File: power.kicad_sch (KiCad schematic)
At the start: 29 parts, among them U201 XC6206PxxxMR, U202 XR76208

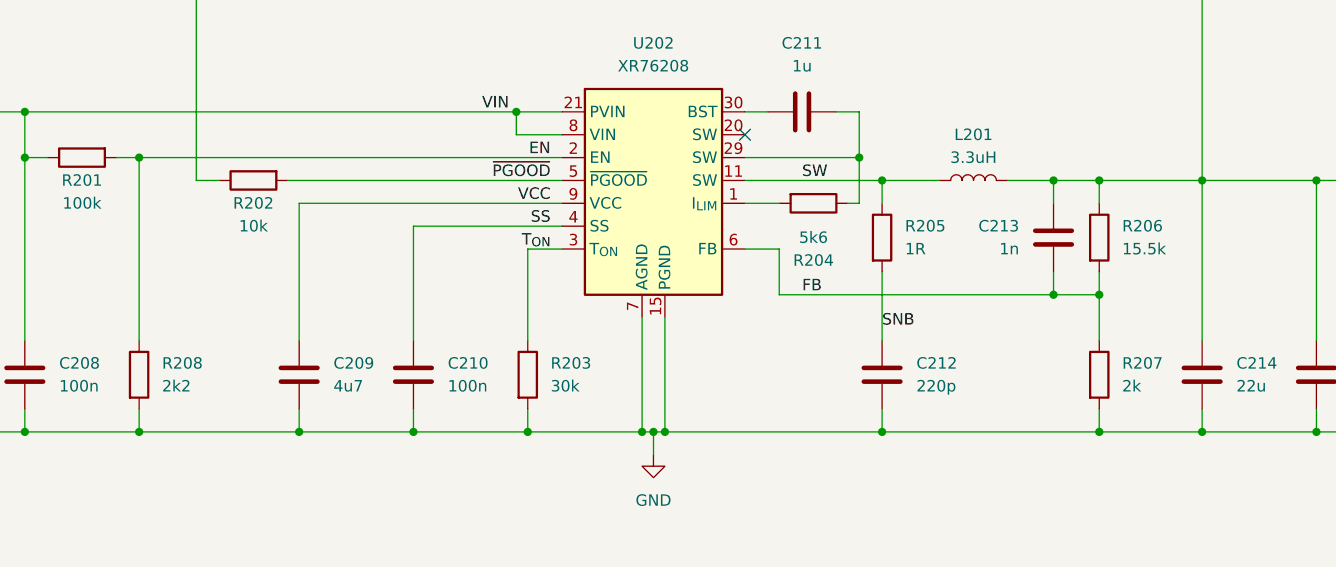
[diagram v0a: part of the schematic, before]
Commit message: Major hardware update: toolhead switching, DC/DC protection, and documentation overhaul
Hardware Changes:
- Replaced reverse polarity protection with 2x PFET toolhead switching (PB2/PA5 control)
- Added SS56 Schottky diode reverse polarity protection for DC/DC converter
- Updated current limit resistor to 5.1kΩ (~10.2A)
- Removed fan control circuitry and JST-XH connector
- Removed internal JST-XH USB port with fuse/protection

Documentation Updates:
- Updated both README files to reflect hardware changes
- Removed all fan control references and configurations
- Updated Klipper configuration examples
- Cleaned up pinout and connector assignments
- Updated technical specifications table
- Fixed table of contents and cross-references
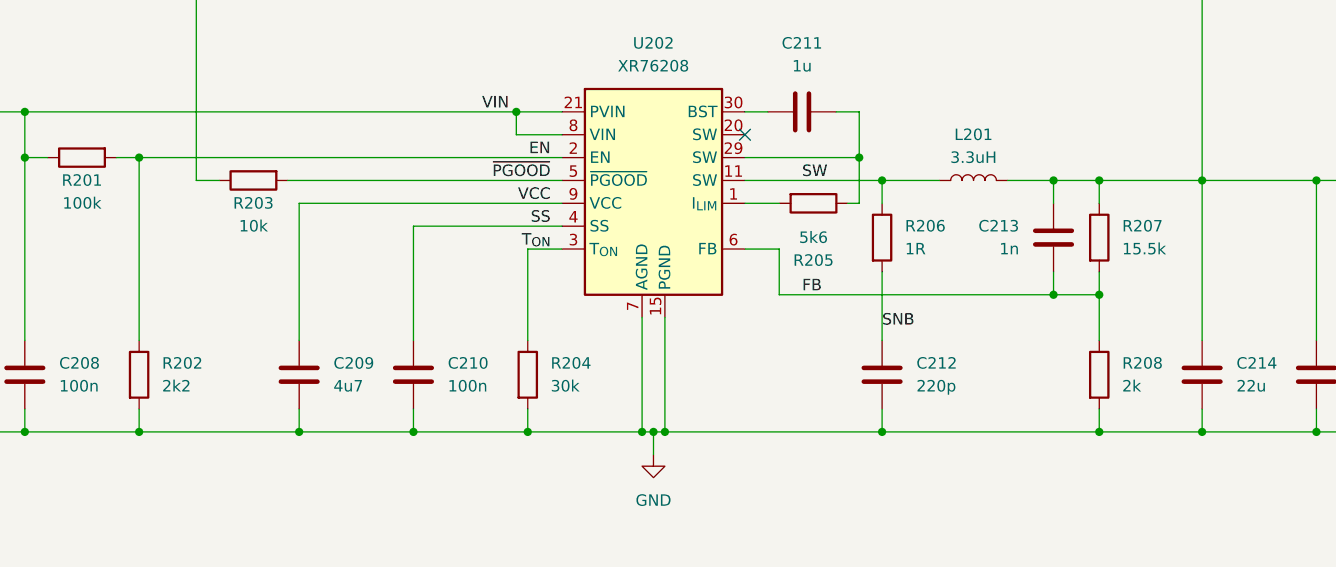
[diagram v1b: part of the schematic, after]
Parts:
- renumbered R208 to R202, R202 to R203, R203 to R204, R204 to R205, R205 to R206, R206 to R207, R207 to R208
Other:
- company: (none) -> Eduard Iten
- title: (none) -> EWS - Power, CANbus and USB HAT for 3D Printers
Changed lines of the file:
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@@
 	(generator_version "9.0")
 	(paper "A4")
+	(title_block
+		(title "EWS - Power, CANbus and USB HAT for 3D Printers")
+		(date "2025-12-03")
+		(rev "1.0")
+		(company "Eduard Iten")
+	)
 	(junction
 		(at 106.68 59.69)
@@
 		(dnp no)
 		(fields_autoplaced yes)
-		(property "Reference" "R206"
+		(property "Reference" "R207"
 			(at 215.9 67.3099 0)
 			(effects
@@
 			(project "EWS"
 				(path "/4ae99543-64c8-472f-befd-04c32f138656/e94b5c4c-885f-4cd2-8976-23421227f36b"
-					(reference "R206")
+					(reference "R207")
 					(unit 1)
 				)
@@
 		(dnp no)
 		(fields_autoplaced yes)
-		(property "Reference" "R208"
+		(property "Reference" "R202"
 			(at 109.22 82.5499 0)
 			(effects
@@
 			(project "EWS"
 				(path "/4ae99543-64c8-472f-befd-04c32f138656/e94b5c4c-885f-4cd2-8976-23421227f36b"
-					(reference "R208")
+					(reference "R202")
 					(unit 1)
 				)
@@
 		(on_board yes)
 		(dnp no)
-		(property "Reference" "R204"
+		(property "Reference" "R205"
 			(at 181.61 71.12 90)
 			(effects
@@
 			(project "EWS"
 				(path "/4ae99543-64c8-472f-befd-04c32f138656/e94b5c4c-885f-4cd2-8976-23421227f36b"
-					(reference "R204")
+					(reference "R205")
 					(unit 1)
 				)
@@
 		(dnp no)
 		(fields_autoplaced yes)
-		(property "Reference" "R207"
+		(property "Reference" "R208"
 			(at 215.9 82.5499 0)
 			(effects
@@
 			(project "EWS"
 				(path "/4ae99543-64c8-472f-befd-04c32f138656/e94b5c4c-885f-4cd2-8976-23421227f36b"
-					(reference "R207")
+					(reference "R208")
 					(unit 1)
 				)
@@
 		(on_board yes)
 		(dnp no)
-		(property "Reference" "R202"
+		(property "Reference" "R203"
 			(at 119.38 64.77 90)
 			(effects
@@
 			(project "EWS"
 				(path "/4ae99543-64c8-472f-befd-04c32f138656/e94b5c4c-885f-4cd2-8976-23421227f36b"
-					(reference "R202")
+					(reference "R203")
 					(unit 1)
 				)
@@
 		(dnp no)
 		(fields_autoplaced yes)
-		(property "Reference" "R203"
+		(property "Reference" "R204"
 			(at 152.4 82.5499 0)
 			(effects
@@
 			(project ""
 				(path "/4ae99543-64c8-472f-befd-04c32f138656/e94b5c4c-885f-4cd2-8976-23421227f36b"
-					(reference "R203")
+					(reference "R204")
 					(unit 1)
 				)
@@
 		(on_board yes)
 		(dnp no)
-		(property "Reference" "R205"
+		(property "Reference" "R206"
 			(at 191.77 67.3099 0)
 			(effects
@@
 			(project "EWS"
 				(path "/4ae99543-64c8-472f-befd-04c32f138656/e94b5c4c-885f-4cd2-8976-23421227f36b"
-					(reference "R205")
+					(reference "R206")
 					(unit 1)
 				)

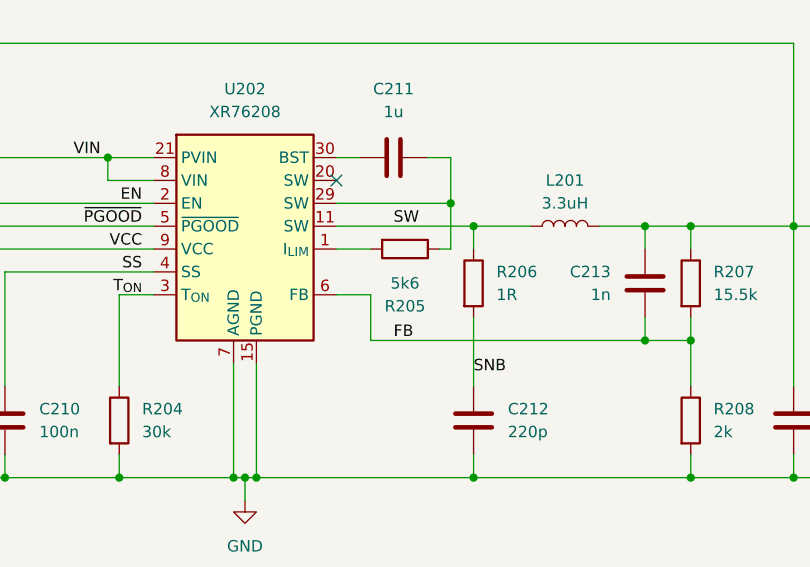
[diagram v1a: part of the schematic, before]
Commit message: Update schema files: conn.kicad_sch and power.kicad_sch
- Updated connector schematic (conn.kicad_sch)
- Updated power schematic (power.kicad_sch)
- Schema changes reflect latest hardware modifications
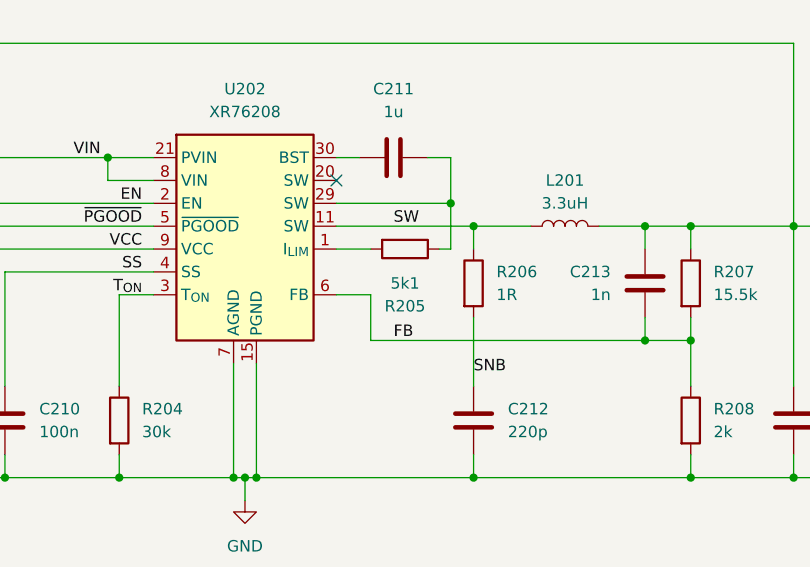
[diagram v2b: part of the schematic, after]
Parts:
- R205: value 5k6 -> 5k1
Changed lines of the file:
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@@
 			)
 		)
-		(property "Value" "5k6"
+		(property "Value" "5k1"
 			(at 181.61 68.58 90)
 			(effects
@@
 			(at 181.61 64.77 0)
 			(effects
+				(font
+					(size 1.27 1.27)
+				)
+				(hide yes)
+			)
+		)
+		(property "Manufacturer Part #" ""
+			(at 181.61 64.77 0)
+			(effects
+				(font
+					(size 1.27 1.27)
+				)
+				(hide yes)
+			)
+		)
+		(property "LCSC Part #" ""
+			(at 181.61 64.77 0)
+			(effects
+				(font
+					(size 1.27 1.27)
+				)
+				(hide yes)
+			)
+		)
+		(property "FT Rotation Offset" ""
+			(at 181.61 64.77 0)
+			(effects

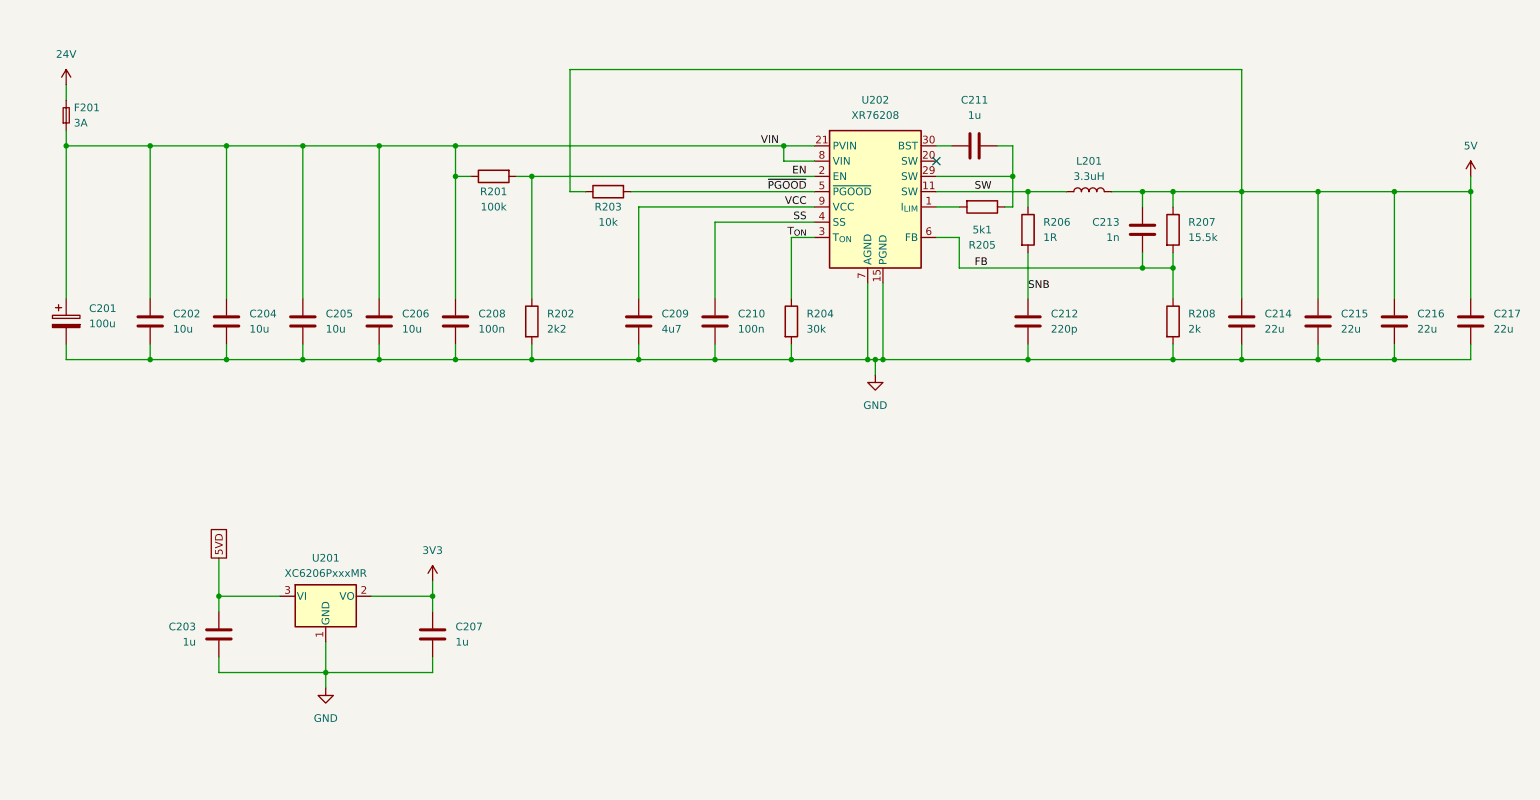
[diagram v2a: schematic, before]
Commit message: Enhanced documentation and final hardware corrections
Documentation Improvements:
- Added comprehensive 'Problems Addressed' section explaining the value proposition
- Covers power supply issues, CAN communication problems, safety concerns, and wiring challenges
- Removed JST-XH internal USB port references from pinout sections
- Corrected via placement specification (DC/DC PGND instead of output)

Hardware Updates:
- Updated schema files with latest component changes
- Added custom footprints for XR76203ELTR-F and heat sink components
- Refined manufacturing guidelines for optimal thermal performance

The documentation now clearly articulates the EWS board's role in solving common
Voron 3D printer control system challenges.
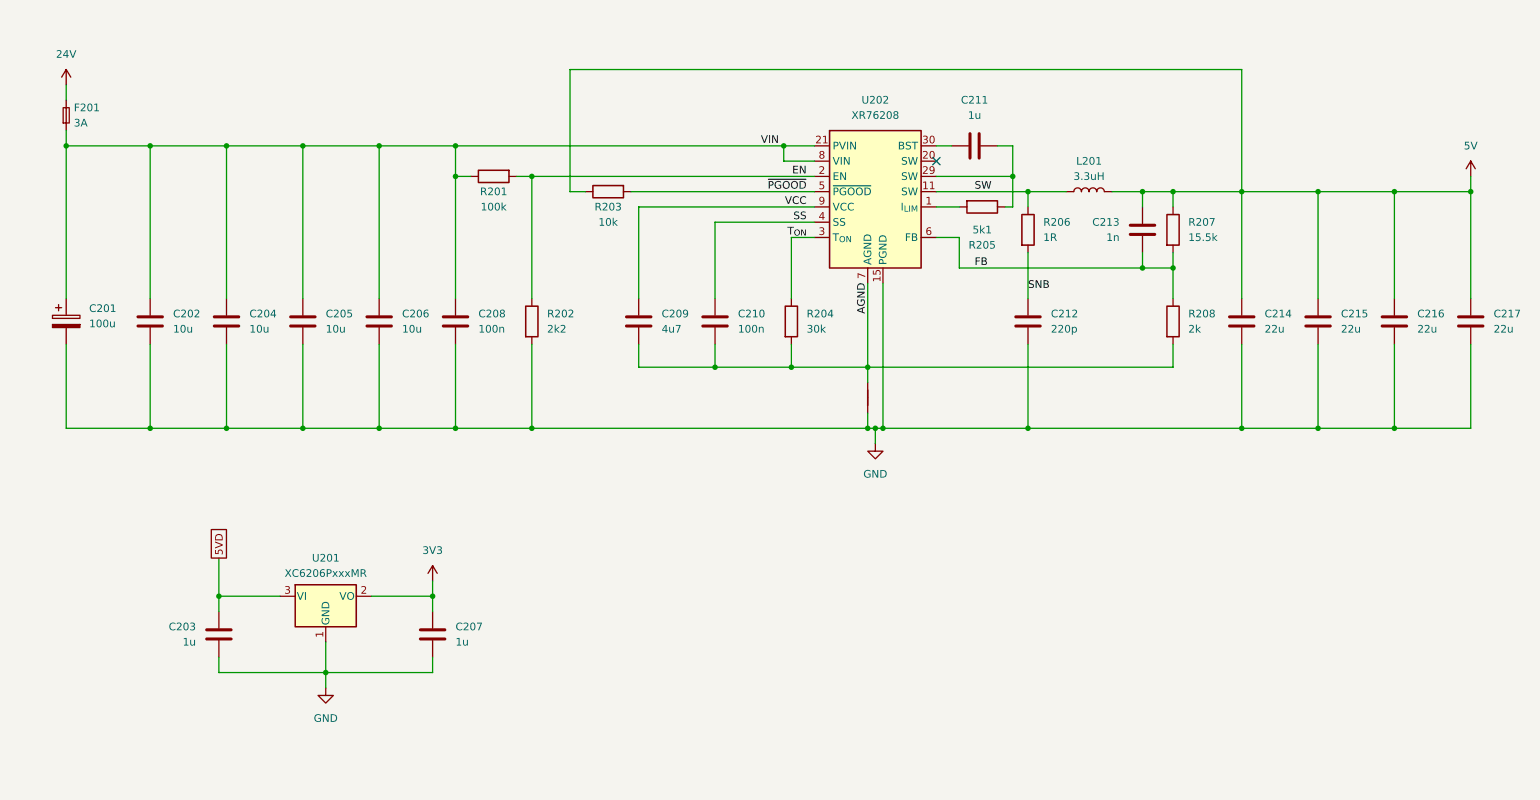
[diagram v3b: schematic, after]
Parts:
- added NT201: NetTie_2, NetTie:NetTie-2_SMD_Pad0.5mm, symbol Device:NetTie_2
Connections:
- net GND: now also NT201.1; no longer C209.2, C210.2, R204.2, R208.2, U202.10 (AGND), U202.31 (AGND), U202.7 (AGND)
- new net AGND: C209.2, C210.2, NT201.2, R204.2, R208.2, U202.10 (AGND), U202.31 (AGND), U202.7 (AGND)

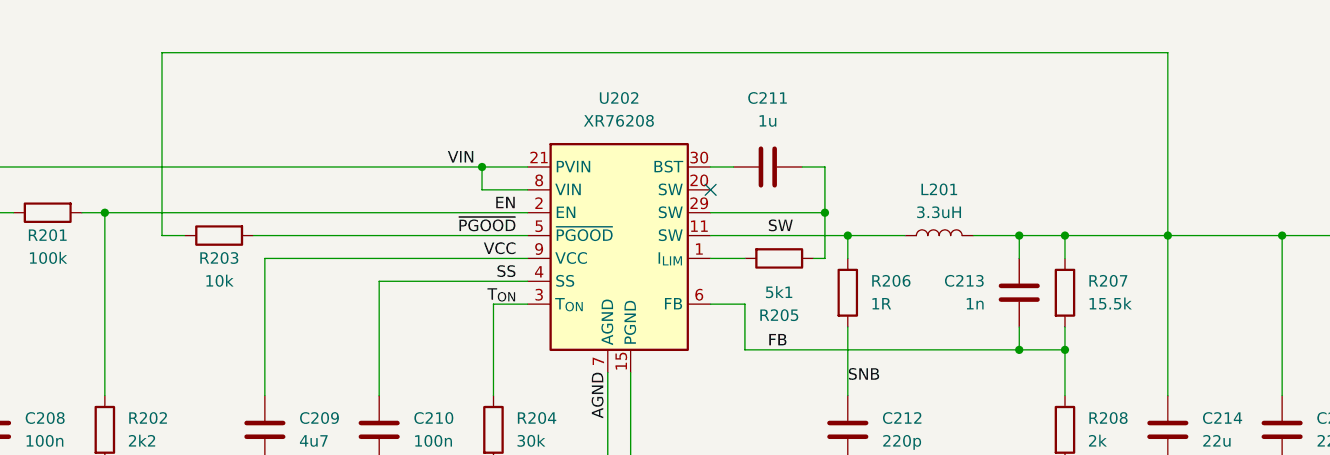
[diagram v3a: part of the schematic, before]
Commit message: EWS Rev 0.1 - Complete design with documentation
Release Features:
- Universal HAT for Raspberry Pi 4/5 and Radxa Rock 5B/5B+
- 8A DC/DC converter with SS56 reverse polarity protection
- Dual toolhead switching via PFETs (PB2/PA5 control)
- Native CAN and USB-CAN bridge support
- USB hub with power delivery for touchscreens
- Comprehensive safety features and thermal management

Hardware:
- STM32G0B1KBU6 MCU with crystal-less design
- MaxLinear XR76208 switching regulator
- MCP2542WFD CAN transceiver with jumper selection
- WCH CH334F USB hub with MTT support
- 2oz copper PCB recommended for thermal performance

Documentation:
- Bilingual documentation (German/English)
- Installation guides with kernel diagnostics
- Klipper configuration examples
- Comprehensive problem statement and solutions
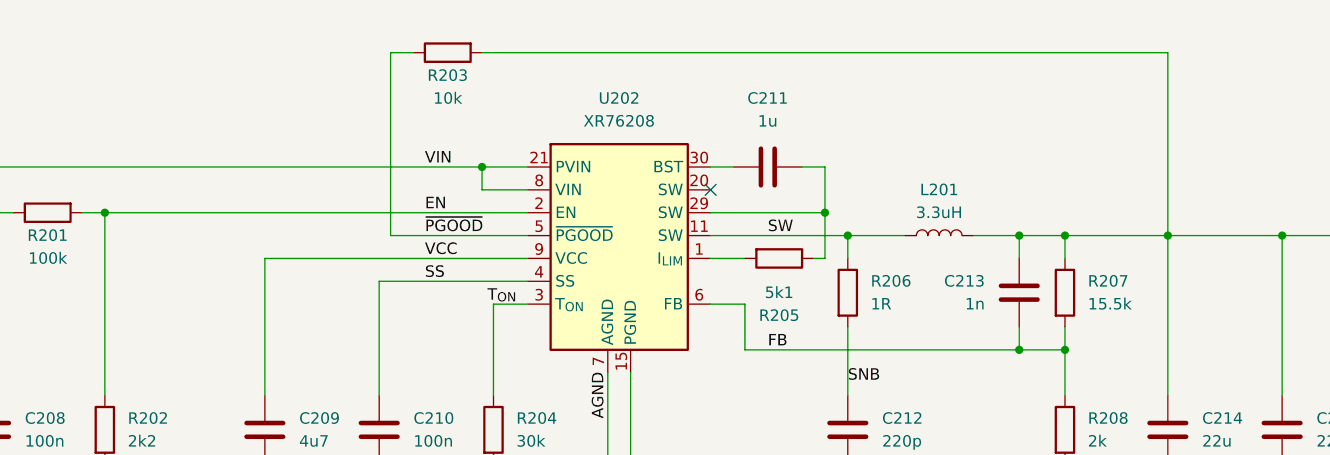
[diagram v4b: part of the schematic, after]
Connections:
- net 5V: now also R203.2; no longer R203.1
- net ~{PGOOD}: now also R203.1; no longer R203.2
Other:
- moved on the sheet: R203
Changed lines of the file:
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@@
-	(wire
-		(pts
-			(xy 123.19 62.23) (xy 153.67 62.23)
-		)
-		(stroke
-			(width 0)
-			(type default)
-		)
-	)
 	(wire
 		(pts
@@
 	(wire
 		(pts
+			(xy 148.59 41.91) (xy 224.79 41.91)
+		)
+		(stroke
+			(width 0)
+			(type default)
+		)
+	)
+	(wire
+		(pts
 			(xy 203.2 62.23) (xy 208.28 62.23)
 		)
@@
 	(wire
 		(pts
-			(xy 113.03 62.23) (xy 113.03 41.91)
+			(xy 138.43 62.23) (xy 138.43 41.91)
 		)
 		(stroke
@@
 	(wire
 		(pts
-			(xy 113.03 41.91) (xy 224.79 41.91)
+			(xy 138.43 41.91) (xy 140.97 41.91)
 		)
 		(stroke
@@
 	(wire
 		(pts
-			(xy 115.57 62.23) (xy 113.03 62.23)
+			(xy 138.43 62.23) (xy 153.67 62.23)
 		)
 		(stroke
@@
 	)
 	(label "~{PGOOD}"
-		(at 152.4 62.23 180)
+		(at 142.24 62.23 0)
 		(effects
 			(font
 				(size 1.27 1.27)
 			)
-			(justify right bottom)
+			(justify left bottom)
 		)
 	)
@@
 	)
 	(label "VCC"
-		(at 152.4 64.77 180)
+		(at 142.24 64.77 0)
 		(effects
 			(font
 				(size 1.27 1.27)
 			)
-			(justify right bottom)
+			(justify left bottom)
 		)
 	)
 	(label "VIN"
-		(at 144.78 54.61 0)
+		(at 142.24 54.61 0)
 		(effects
 			(font
@@
 	)
 	(label "EN"
-		(at 152.4 59.69 180)
+		(at 142.24 59.69 0)
 		(effects
 			(font
 				(size 1.27 1.27)
 			)
-			(justify right bottom)
+			(justify left bottom)
 		)
 	)
@@
 	)
 	(label "SS"
-		(at 152.4 67.31 180)
+		(at 142.24 67.31 0)
 		(effects
 			(font
 				(size 1.27 1.27)
 			)
-			(justify right bottom)
+			(justify left bottom)
 		)
 	)
@@
 	(symbol
 		(lib_id "Device:R")
-		(at 119.38 62.23 90)
+		(at 144.78 41.91 90)
 		(mirror x)
 		(unit 1)
@@
 		(dnp no)
 		(property "Reference" "R203"
-			(at 119.38 64.77 90)
+			(at 144.78 44.45 90)
 			(effects
 				(font
@@
 		)
 		(property "Value" "10k"
-			(at 119.38 67.31 90)
+			(at 144.78 46.99 90)
 			(effects
 				(font
@@
 		)
 		(property "Footprint" "Resistor_SMD:R_0402_1005Metric"
-			(at 119.38 60.452 90)
+			(at 144.78 40.132 90)
 			(effects
 				(font
@@
 		)
 		(property "Datasheet" "~"
-			(at 119.38 62.23 0)
+			(at 144.78 41.91 0)
 			(effects
 				(font
@@
 		)
 		(property "Description" "Resistor"
-			(at 119.38 62.23 0)
-			(effects
-				(font
+			(at 144.78 41.91 0)
+			(effects
+				(font
